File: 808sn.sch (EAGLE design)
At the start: 72 parts, among them IC1 TL072P, IC2 TL072P, Q1 BC546A, Q45 BC546A, Q46 BC556, Q47 BC546A, Q48 BC546A, Q49 BC546A

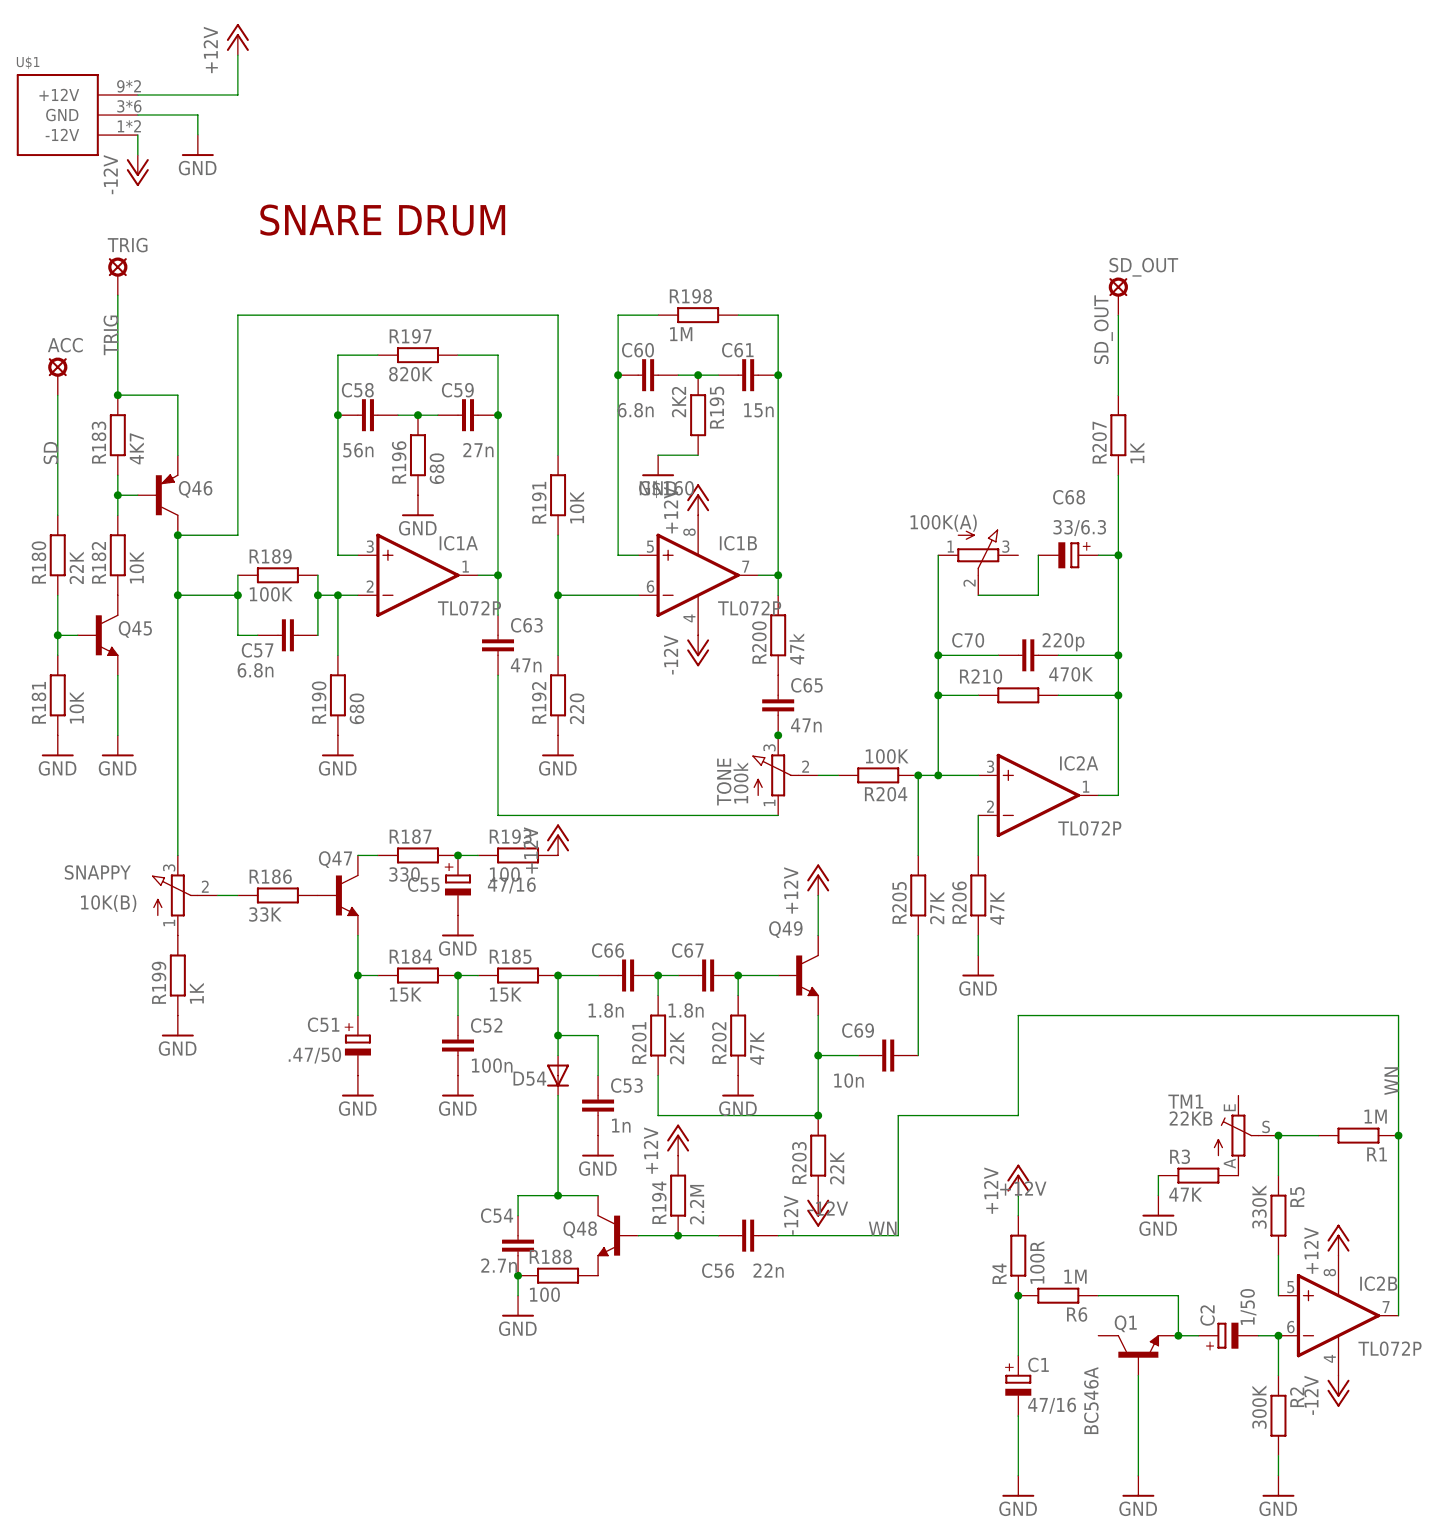
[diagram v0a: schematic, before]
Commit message: opamps flipped, working on layout
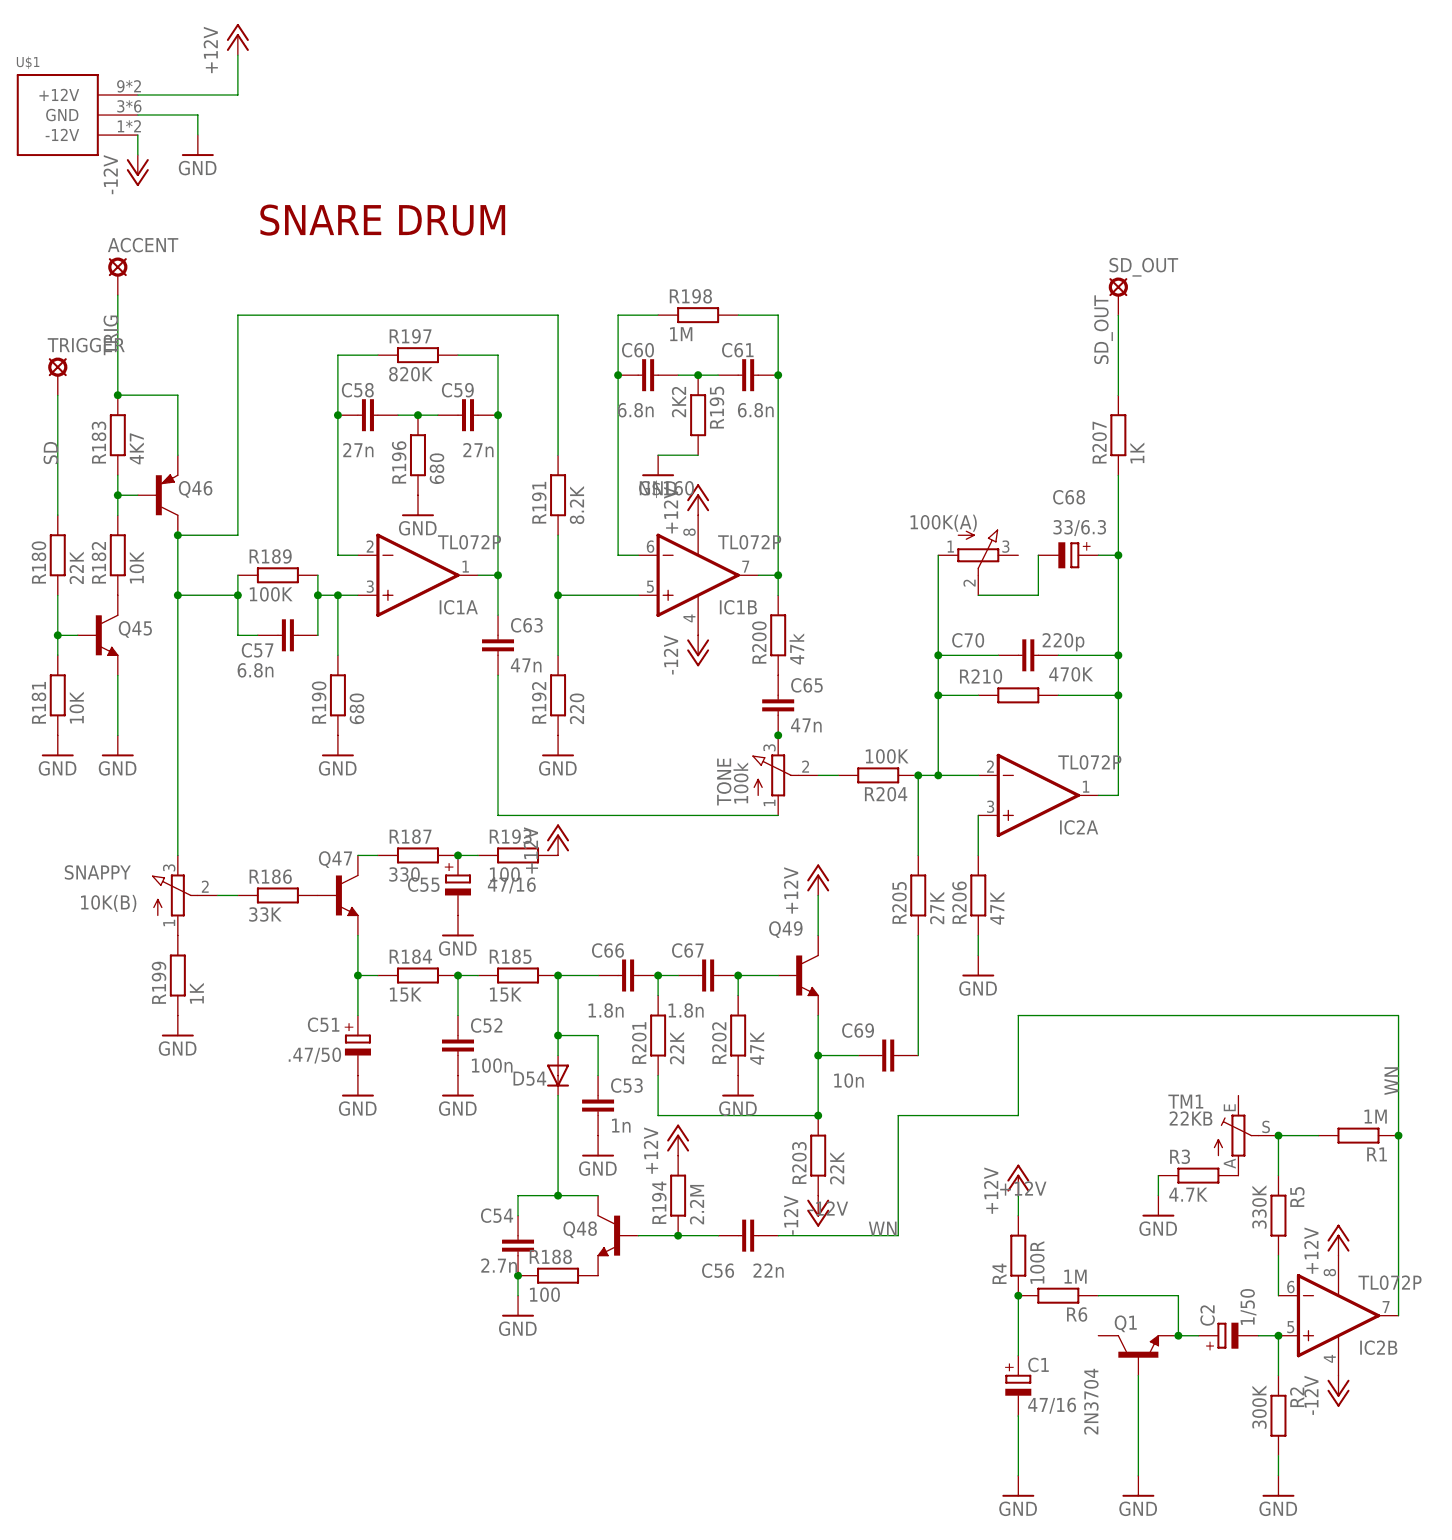
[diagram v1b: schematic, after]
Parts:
- C58: value 56n -> 27n
- C61: value 15n -> 6.8n
- Q1: value BC546A -> 2N3704; device transistor-npn:BC546A -> transistor:2N3704
- R191: value 10K -> 8.2K
- R3: value 47K -> 4.7K
- renumbered ACC to TRIGGER, TRIG to ACCENT
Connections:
- removed net N$53: IC2A.-IN, R206.2
- removed net N$708: IC2B.+IN, R5.2
- removed net N$712: C2.-, IC2B.-IN, R2.1
- new net N$1: IC2A.+IN, R206.2
- new net N$2: C2.-, IC2B.+IN, R2.1
- new net N$3: IC2B.-IN, R5.2
- net N$11: now also IC1A.-IN; no longer IC1A.+IN
- net N$16: now also IC1B.+IN; no longer IC1B.-IN
- net N$160: now also IC1B.-IN; no longer IC1B.+IN
- net N$35: now also IC2A.-IN; no longer IC2A.+IN
- net N$8: now also IC1A.+IN; no longer IC1A.-IN
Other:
- moved on the sheet: IC1A, IC1B, IC2A, IC2B
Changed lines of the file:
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@@
 <part name="GND3" library="supply1" deviceset="GND" device=""/>
 <part name="GND4" library="supply1" deviceset="GND" device=""/>
-<part name="C58" library="TR808clone" deviceset="C-EU" device="050-024X044" value="56n"/>
+<part name="C58" library="TR808clone" deviceset="C-EU" device="050-024X044" value="27n"/>
 <part name="C59" library="TR808clone" deviceset="C-EU" device="050-024X044" value="27n"/>
 <part name="C57" library="TR808clone" deviceset="C-EU" device="4MM_PITCH" value="6.8n"/>
@@
 <part name="GND6" library="supply1" deviceset="GND" device=""/>
 <part name="C60" library="TR808clone" deviceset="C-EU" device="4MM_PITCH" value="6.8n"/>
-<part name="C61" library="TR808clone" deviceset="C-EU" device="4MM_PITCH" value="15n"/>
+<part name="C61" library="TR808clone" deviceset="C-EU" device="4MM_PITCH" value="6.8n"/>
 <part name="R195" library="TR808clone" deviceset="R-EU_" device="0207/5V" value="2K2"/>
 <part name="R198" library="TR808clone" deviceset="R-EU_" device="0207/5V" value="1M"/>
 <part name="GND7" library="supply1" deviceset="GND" device=""/>
 <part name="R192" library="TR808clone" deviceset="R-EU_" device="0207/5V" value="220"/>
-<part name="R191" library="TR808clone" deviceset="R-EU_" device="0207/5V" value="10K"/>
+<part name="R191" library="TR808clone" deviceset="R-EU_" device="0207/5V" value="8.2K"/>
 <part name="GND8" library="supply1" deviceset="GND" device=""/>
 <part name="C63" library="TR808clone" deviceset="C-EU" device="050-024X044" value="47n"/>
@@
 <part name="V1" library="supply1" deviceset="GND" device=""/>
 <part name="V2" library="supply1" deviceset="GND" device=""/>
-<part name="R3" library="TR808clone" deviceset="R-EU_" device="0207/5V" value="47K"/>
+<part name="R3" library="TR808clone" deviceset="R-EU_" device="0207/5V" value="4.7K"/>
 <part name="V3" library="supply1" deviceset="GND" device=""/>
 <part name="C1" library="TR808clone" deviceset="CPOL-EU" device="E2.5-5" value="47/16"/>
@@
 <part name="R5" library="TR808clone" deviceset="R-EU_" device="0207/5V" value="330K"/>
 <part name="R6" library="TR808clone" deviceset="R-EU_" device="0207/5V" value="1M"/>
-<part name="Q1" library="transistor-npn" deviceset="BC546*" device="" technology="A"/>
+<part name="Q1" library="transistor" deviceset="2N3704" device=""/>
 <part name="TM1" library="pot" deviceset="TRIM_1234-" device="S64YW" value="22KB"/>
 <part name="SD_OUT" library="solpad" deviceset="LSP11" device=""/>
-<part name="ACC" library="solpad" deviceset="LSP11" device=""/>
-<part name="TRIG" library="solpad" deviceset="LSP11" device=""/>
+<part name="TRIGGER" library="solpad" deviceset="LSP11" device=""/>
+<part name="ACCENT" library="solpad" deviceset="LSP11" device=""/>
 <part name="P+1" library="supply1" deviceset="+12V" device=""/>
 <part name="P-1" library="supply1" deviceset="-12V" device=""/>
@@
 </instance>
 <instance part="SD_OUT" gate="1" x="137.16" y="106.68"/>
-<instance part="ACC" gate="1" x="2.54" y="96.52"/>
-<instance part="TRIG" gate="1" x="10.16" y="109.22"/>
+<instance part="TRIGGER" gate="1" x="2.54" y="96.52"/>
+<instance part="ACCENT" gate="1" x="10.16" y="109.22"/>
 <instance part="P+1" gate="1" x="25.4" y="139.7"/>
 <instance part="P-1" gate="1" x="12.7" y="121.92"/>
@@
 <instance part="GND1" gate="1" x="20.32" y="124.46"/>
 <instance part="P+7" gate="1" x="81.28" y="0"/>
-<instance part="IC1" gate="A" x="48.26" y="71.12"/>
-<instance part="IC1" gate="B" x="83.82" y="71.12"/>
-<instance part="IC2" gate="A" x="127" y="43.18"/>
-<instance part="IC2" gate="B" x="165.1" y="-22.86"/>
+<instance part="IC1" gate="A" x="48.26" y="71.12" rot="MR180"/>
+<instance part="IC1" gate="B" x="83.82" y="71.12" rot="MR180"/>
+<instance part="IC2" gate="A" x="127" y="43.18" rot="MR180"/>
+<instance part="IC2" gate="B" x="165.1" y="-22.86" rot="MR180"/>
 <instance part="IC1" gate="P" x="83.82" y="71.12"/>
 <instance part="IC2" gate="P" x="165.1" y="-22.86"/>
@@
 <label x="10.16" y="99.06" size="1.778" layer="95" rot="R90"/>
 <junction x="10.16" y="93.98"/>
-<pinref part="TRIG" gate="1" pin="MP"/>
+<pinref part="ACCENT" gate="1" pin="MP"/>
 </segment>
 </net>
@@
 <wire x1="35.56" y1="68.58" x2="38.1" y2="68.58" width="0.1524" layer="91"/>
 <pinref part="R189" gate="G$1" pin="2"/>
-<wire x1="38.1" y1="68.58" x2="40.64" y2="68.58" width="0.1524" layer="91"/>
 <wire x1="35.56" y1="71.12" x2="35.56" y2="68.58" width="0.1524" layer="91"/>
 <pinref part="R190" gate="G$1" pin="2"/>
 <wire x1="38.1" y1="68.58" x2="38.1" y2="60.96" width="0.1524" layer="91"/>
+<junction x="35.56" y="68.58"/>
+<pinref part="IC1" gate="A" pin="+IN"/>
+<wire x1="40.64" y1="68.58" x2="38.1" y2="68.58" width="0.1524" layer="91"/>
 <junction x="38.1" y="68.58"/>
-<junction x="35.56" y="68.58"/>
-<pinref part="IC1" gate="A" pin="-IN"/>
 </segment>
 </net>
@@
 <pinref part="C58" gate="G$1" pin="1"/>
 <wire x1="38.1" y1="91.44" x2="38.1" y2="73.66" width="0.1524" layer="91"/>
-<wire x1="38.1" y1="73.66" x2="40.64" y2="73.66" width="0.1524" layer="91"/>
 <pinref part="R197" gate="G$1" pin="1"/>
 <wire x1="43.18" y1="99.06" x2="38.1" y2="99.06" width="0.1524" layer="91"/>
 <wire x1="38.1" y1="99.06" x2="38.1" y2="91.44" width="0.1524" layer="91"/>
 <junction x="38.1" y="91.44"/>
-<pinref part="IC1" gate="A" pin="+IN"/>
+<pinref part="IC1" gate="A" pin="-IN"/>
+<wire x1="40.64" y1="73.66" x2="38.1" y2="73.66" width="0.1524" layer="91"/>
 </segment>
 </net>
@@
 <pinref part="R192" gate="G$1" pin="2"/>
 <wire x1="66.04" y1="76.2" x2="66.04" y2="68.58" width="0.1524" layer="91"/>
+<pinref part="IC1" gate="B" pin="+IN"/>
 <wire x1="66.04" y1="68.58" x2="66.04" y2="60.96" width="0.1524" layer="91"/>
 <wire x1="76.2" y1="68.58" x2="66.04" y2="68.58" width="0.1524" layer="91"/>
 <junction x="66.04" y="68.58"/>
-<pinref part="IC1" gate="B" pin="-IN"/>
 </segment>
 </net>
@@
 <segment>
 <pinref part="R204" gate="G$1" pin="1"/>
-<wire x1="119.38" y1="45.72" x2="114.3" y2="45.72" width="0.1524" layer="91"/>
 <pinref part="R205" gate="G$1" pin="2"/>
 <wire x1="114.3" y1="45.72" x2="111.76" y2="45.72" width="0.1524" layer="91"/>
@@
 <wire x1="114.3" y1="60.96" x2="114.3" y2="73.66" width="0.1524" layer="91"/>
 <junction x="111.76" y="45.72"/>
-<junction x="114.3" y="45.72"/>
 <junction x="114.3" y="55.88"/>
 <junction x="114.3" y="60.96"/>
-<pinref part="IC2" gate="A" pin="+IN"/>
+<pinref part="IC2" gate="A" pin="-IN"/>
+<wire x1="119.38" y1="45.72" x2="114.3" y2="45.72" width="0.1524" layer="91"/>
+<junction x="114.3" y="45.72"/>
 </segment>
 </net>
@@
 <pinref part="R205" gate="G$1" pin="1"/>
 <wire x1="111.76" y1="10.16" x2="111.76" y2="25.4" width="0.1524" layer="91"/>
-</segment>
-</net>
-<net name="N$53" class="0">
-<segment>
-<pinref part="R206" gate="G$1" pin="2"/>
-<wire x1="119.38" y1="40.64" x2="119.38" y2="35.56" width="0.1524" layer="91"/>
-<pinref part="IC2" gate="A" pin="-IN"/>
 </segment>
 </net>
@@
 <wire x1="2.54" y1="78.74" x2="2.54" y2="93.98" width="0.1524" layer="91"/>
 <label x="2.54" y="85.09" size="1.778" layer="95" rot="R90"/>
-<pinref part="ACC" gate="1" pin="MP"/>
+<pinref part="TRIGGER" gate="1" pin="MP"/>
 </segment>
 </net>
@@
 <wire x1="78.74" y1="104.14" x2="73.66" y2="104.14" width="0.1524" layer="91"/>
 <wire x1="73.66" y1="104.14" x2="73.66" y2="96.52" width="0.1524" layer="91"/>
-<wire x1="76.2" y1="73.66" x2="73.66" y2="73.66" width="0.1524" layer="91"/>
 <wire x1="73.66" y1="73.66" x2="73.66" y2="96.52" width="0.1524" layer="91"/>
 <junction x="73.66" y="96.52"/>
-<pinref part="IC1" gate="B" pin="+IN"/>
 <label x="76.2" y="81.28" size="1.778" layer="95"/>
+<pinref part="IC1" gate="B" pin="-IN"/>
+<wire x1="76.2" y1="73.66" x2="73.66" y2="73.66" width="0.1524" layer="91"/>
 </segment>
 </net>
@@
 <pinref part="TM1" gate="1" pin="S"/>
 <junction x="157.48" y="0"/>
-</segment>
-</net>
-<net name="N$708" class="0">
-<segment>
-<wire x1="157.48" y1="-15.24" x2="157.48" y2="-20.32" width="0.1524" layer="91"/>
-<pinref part="R5" gate="G$1" pin="2"/>
-<pinref part="IC2" gate="B" pin="+IN"/>
 </segment>
 </net>
@@
 </segment>
 </net>
-<net name="N$712" class="0">
-<segment>
-<pinref part="C2" gate="G$1" pin="-"/>
-<wire x1="154.94" y1="-25.4" x2="157.48" y2="-25.4" width="0.1524" layer="91"/>
-<pinref part="R2" gate="G$1" pin="1"/>
-<wire x1="157.48" y1="-30.48" x2="157.48" y2="-25.4" width="0.1524" layer="91"/>
-<pinref part="IC2" gate="B" pin="-IN"/>
-<junction x="157.48" y="-25.4"/>
-</segment>
-</net>
 <net name="+12V" class="0">
 <segment>
@@
 </segment>
 </net>
+<net name="N$1" class="0">
+<segment>
+<pinref part="IC2" gate="A" pin="+IN"/>
+<pinref part="R206" gate="G$1" pin="2"/>
+<wire x1="119.38" y1="40.64" x2="119.38" y2="35.56" width="0.1524" layer="91"/>
+</segment>
+</net>
+<net name="N$2" class="0">
+<segment>
+<pinref part="IC2" gate="B" pin="+IN"/>
+<pinref part="C2" gate="G$1" pin="-"/>
+<wire x1="157.48" y1="-25.4" x2="154.94" y2="-25.4" width="0.1524" layer="91"/>
+<pinref part="R2" gate="G$1" pin="1"/>
+<wire x1="157.48" y1="-25.4" x2="157.48" y2="-30.48" width="0.1524" layer="91"/>
+<junction x="157.48" y="-25.4"/>
+</segment>
+</net>
+<net name="N$3" class="0">
+<segment>
+<pinref part="IC2" gate="B" pin="-IN"/>
+<pinref part="R5" gate="G$1" pin="2"/>
+<wire x1="157.48" y1="-20.32" x2="157.48" y2="-15.24" width="0.1524" layer="91"/>
+</segment>
+</net>
